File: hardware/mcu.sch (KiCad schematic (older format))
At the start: 4 parts

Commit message: HW: change tm4c1294ncpdt to kcpdt; change LT3487 to 3471
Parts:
- removed U? (x4): TM4C1294NCPDT, symbol TM4C1294NCPDT
- added U? (x4): TM4C1294KCPDT, symbol TM4C1294KCPDT
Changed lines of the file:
@@
 Text HLabel 10400 2950 0    60   Output ~ 0
 PWM2
-$Comp
-L TM4C1294NCPDT U?
-U 1 1 597FCC05
-P 1450 2650
-F 0 "U?" H 1400 1000 59  0000 C CNN
-F 1 "TM4C1294NCPDT" H 1450 4400 59  0000 C CNN
-F 2 "" H 1400 1400 59  0000 C CNN
-F 3 "" H 1400 1400 59  0000 C CNN
-	1    1450 2650
-	1    0    0    -1
-$EndComp
-$Comp
-L TM4C1294NCPDT U?
-U 2 1 597FCCB0
-P 4400 2350
-F 0 "U?" H 4400 1050 59  0000 C CNN
-F 1 "TM4C1294NCPDT" H 4400 3500 59  0000 C CNN
-F 2 "" H 4350 1100 59  0000 C CNN
-F 3 "" H 4350 1100 59  0000 C CNN
-	2    4400 2350
-	1    0    0    -1
-$EndComp
-$Comp
-L TM4C1294NCPDT U?
-U 3 1 597FCD49
-P 6750 1700
-F 0 "U?" H 6800 1250 59  0000 C CNN
-F 1 "TM4C1294NCPDT" H 6800 2100 59  0000 C CNN
-F 2 "" H 6700 450 59  0000 C CNN
-F 3 "" H 6700 450 59  0000 C CNN
-	3    6750 1700
-	1    0    0    -1
-$EndComp
-$Comp
-L TM4C1294NCPDT U?
-U 4 1 597FCDA0
-P 9100 2300
-F 0 "U?" H 9100 1100 59  0000 C CNN
-F 1 "TM4C1294NCPDT" H 9100 3350 59  0000 C CNN
-F 2 "" H 9050 1050 59  0000 C CNN
-F 3 "" H 9050 1050 59  0000 C CNN
-	4    9100 2300
-	1    0    0    -1
-$EndComp
 Wire Wire Line
 	9700 1350 9800 1350
@@
 Text Notes 6000 6350 2    197  ~ 0
 STATUS LEDs
+$Comp
+L TM4C1294KCPDT U?
+U 1 1 59940BF1
+P 1800 2600
+F 0 "U?" H 1750 950 59  0000 C CNN
+F 1 "TM4C1294KCPDT" H 1800 4350 59  0000 C CNN
+F 2 "" H 1750 1350 59  0000 C CNN
+F 3 "" H 1750 1350 59  0000 C CNN
+	1    1800 2600
+	1    0    0    -1
+$EndComp
+$Comp
+L TM4C1294KCPDT U?
+U 2 1 59940C7A
+P 3800 2200
+F 0 "U?" H 3800 850 59  0000 C CNN
+F 1 "TM4C1294KCPDT" H 3800 3400 59  0000 C CNN
+F 2 "" H 3750 950 59  0000 C CNN
+F 3 "" H 3750 950 59  0000 C CNN
+	2    3800 2200
+	1    0    0    -1
+$EndComp
+$Comp
+L TM4C1294KCPDT U?
+U 3 1 59940CC3
+P 6100 2250
+F 0 "U?" H 6150 1750 59  0000 C CNN
+F 1 "TM4C1294KCPDT" H 6150 2700 59  0000 C CNN
+F 2 "" H 6050 1000 59  0000 C CNN
+F 3 "" H 6050 1000 59  0000 C CNN
+	3    6100 2250
+	1    0    0    -1
+$EndComp
+$Comp
+L TM4C1294KCPDT U?
+U 4 1 59940D20
+P 9100 2300
+F 0 "U?" H 9100 1100 59  0000 C CNN
+F 1 "TM4C1294KCPDT" H 9100 3400 59  0000 C CNN
+F 2 "" H 9050 1050 59  0000 C CNN
+F 3 "" H 9050 1050 59  0000 C CNN
+	4    9100 2300
+	1    0    0    -1
+$EndComp
 $EndSCHEMATC

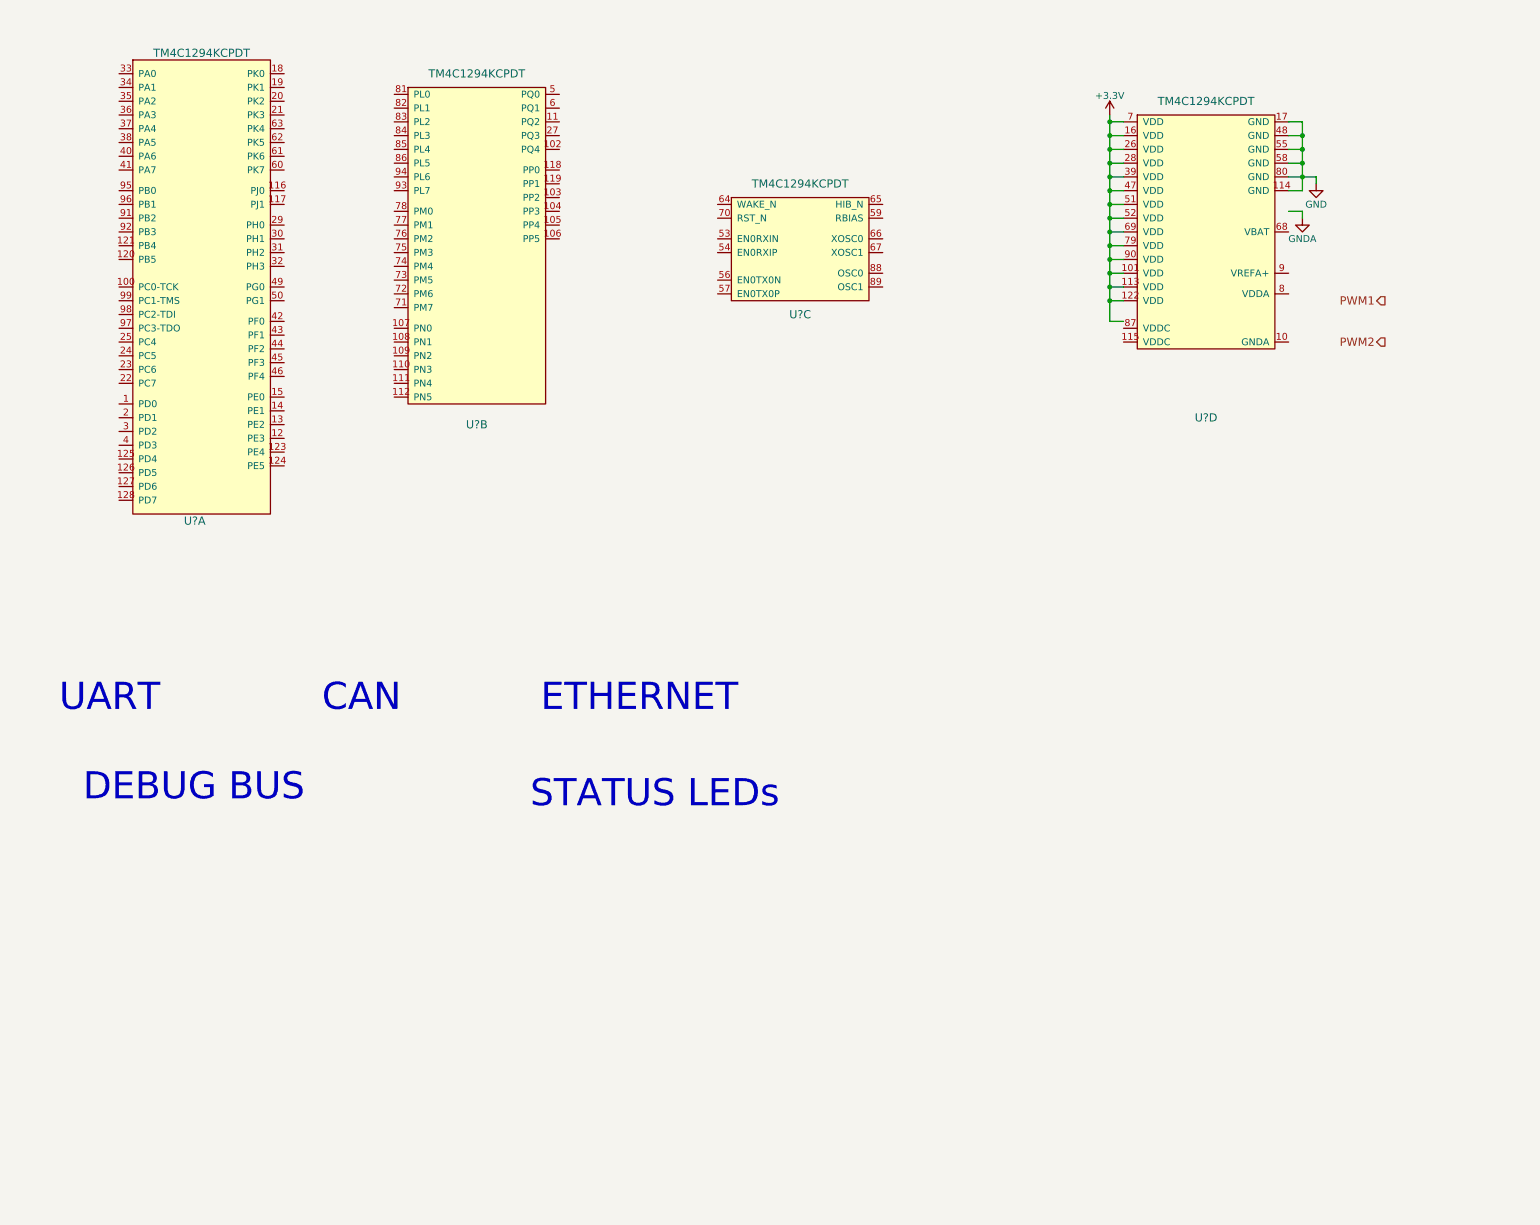
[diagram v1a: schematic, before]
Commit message: cleaned up h-bridge; added digital isolators
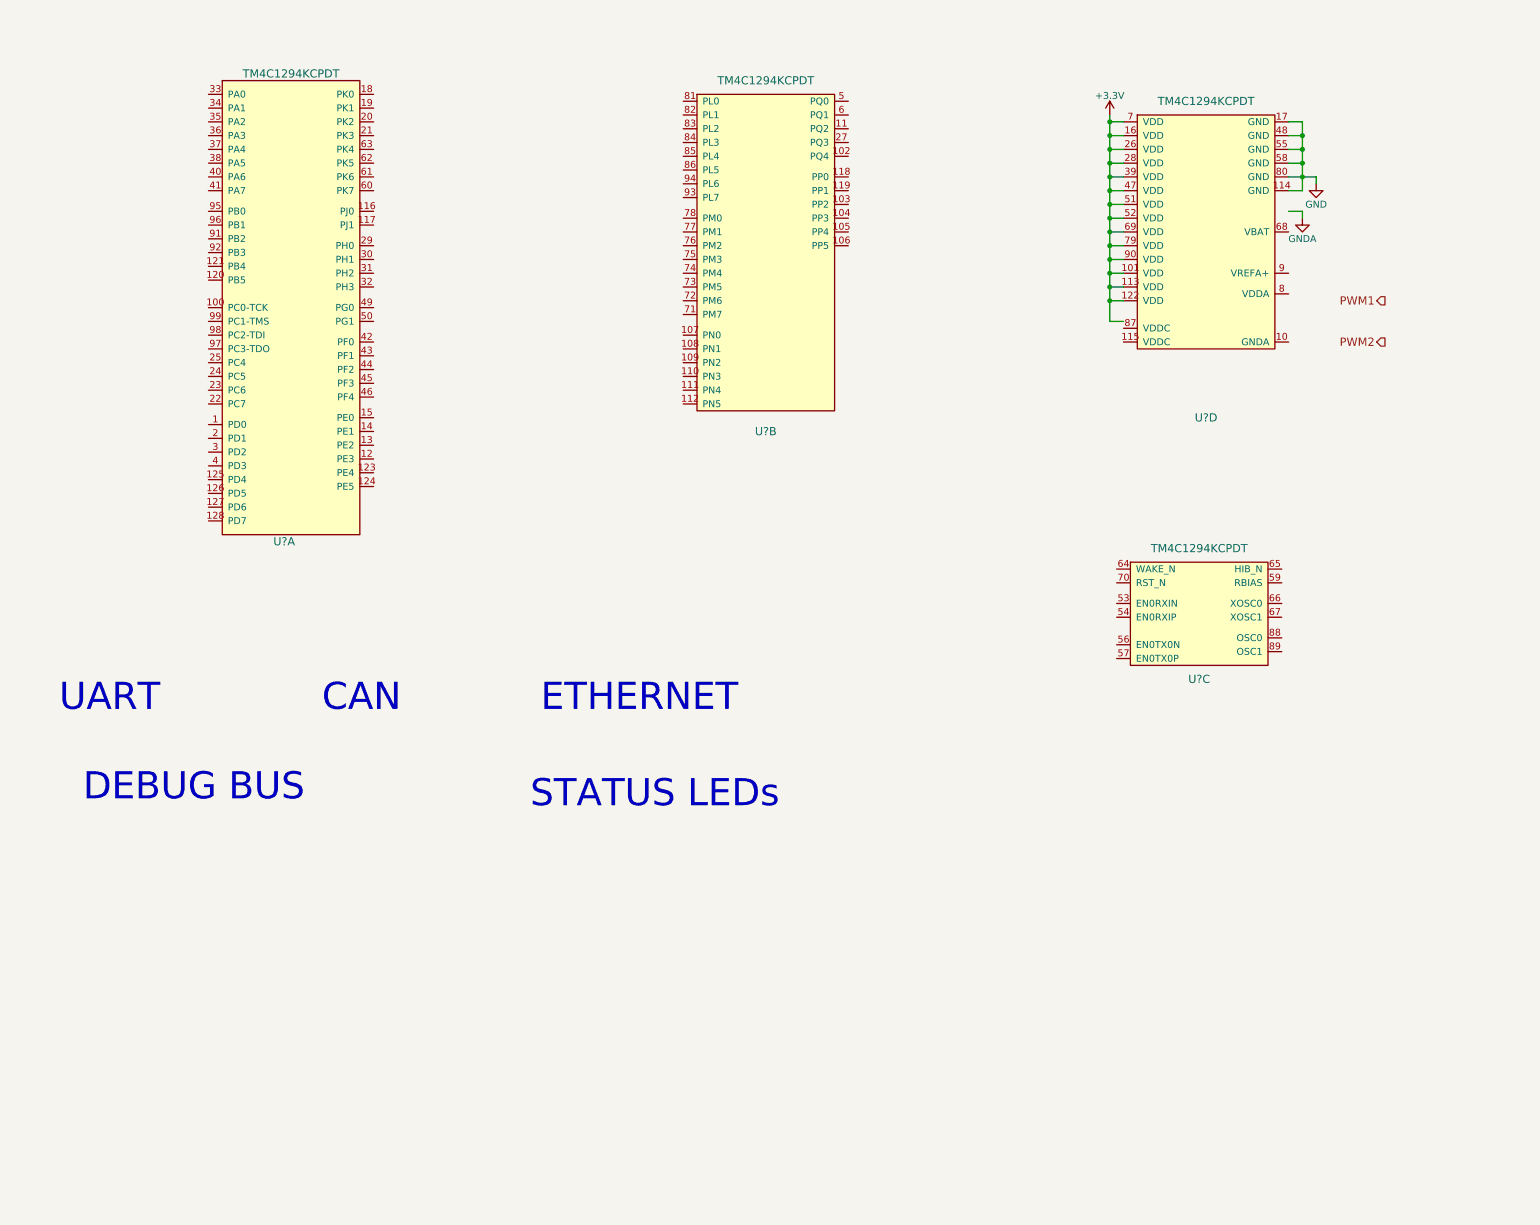
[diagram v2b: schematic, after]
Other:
- moved on the sheet: U?A, U?B, U?C
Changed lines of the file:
@@
 Connection ~ 9800 1450
 $Comp
-L GND #PWR?
+L GND #PWR07
 U 1 1 5983EA5A
 P 9900 1800
-F 0 "#PWR?" H 9900 1550 50  0001 C CNN
+F 0 "#PWR07" H 9900 1550 50  0001 C CNN
 F 1 "GND" H 9900 1650 50  0000 C CNN
 F 2 "" H 9900 1800 50  0000 C CNN
@@
 	9800 2000 9800 2050
 $Comp
-L GNDA #PWR?
+L GNDA #PWR08
 U 1 1 5983EB4E
 P 9800 2050
-F 0 "#PWR?" H 9800 1800 50  0001 C CNN
+F 0 "#PWR08" H 9800 1800 50  0001 C CNN
 F 1 "GNDA" H 9800 1900 50  0000 C CNN
 F 2 "" H 9800 2050 50  0000 C CNN
@@
 $EndComp
 $Comp
-L +3.3V #PWR?
+L +3.3V #PWR09
 U 1 1 5983EC7E
 P 8400 1300
-F 0 "#PWR?" H 8400 1150 50  0001 C CNN
+F 0 "#PWR09" H 8400 1150 50  0001 C CNN
 F 1 "+3.3V" H 8400 1440 50  0000 C CNN
 F 2 "" H 8400 1300 50  0000 C CNN
@@
 L TM4C1294KCPDT U?
 U 1 1 59940BF1
-P 1800 2600
-F 0 "U?" H 1750 950 59  0000 C CNN
-F 1 "TM4C1294KCPDT" H 1800 4350 59  0000 C CNN
-F 2 "" H 1750 1350 59  0000 C CNN
-F 3 "" H 1750 1350 59  0000 C CNN
-	1    1800 2600
+P 2450 2750
+F 0 "U?" H 2400 1100 59  0000 C CNN
+F 1 "TM4C1294KCPDT" H 2450 4500 59  0000 C CNN
+F 2 "" H 2400 1500 59  0000 C CNN
+F 3 "" H 2400 1500 59  0000 C CNN
+	1    2450 2750
 	1    0    0    -1
 $EndComp
@@
 L TM4C1294KCPDT U?
 U 2 1 59940C7A
-P 3800 2200
-F 0 "U?" H 3800 850 59  0000 C CNN
-F 1 "TM4C1294KCPDT" H 3800 3400 59  0000 C CNN
-F 2 "" H 3750 950 59  0000 C CNN
-F 3 "" H 3750 950 59  0000 C CNN
-	2    3800 2200
+P 5900 2250
+F 0 "U?" H 5900 900 59  0000 C CNN
+F 1 "TM4C1294KCPDT" H 5900 3450 59  0000 C CNN
+F 2 "" H 5850 1000 59  0000 C CNN
+F 3 "" H 5850 1000 59  0000 C CNN
+	2    5900 2250
 	1    0    0    -1
 $EndComp
@@
 L TM4C1294KCPDT U?
 U 3 1 59940CC3
-P 6100 2250
-F 0 "U?" H 6150 1750 59  0000 C CNN
-F 1 "TM4C1294KCPDT" H 6150 2700 59  0000 C CNN
-F 2 "" H 6050 1000 59  0000 C CNN
-F 3 "" H 6050 1000 59  0000 C CNN
-	3    6100 2250
+P 9000 4900
+F 0 "U?" H 9050 4400 59  0000 C CNN
+F 1 "TM4C1294KCPDT" H 9050 5350 59  0000 C CNN
+F 2 "" H 8950 3650 59  0000 C CNN
+F 3 "" H 8950 3650 59  0000 C CNN
+	3    9000 4900
 	1    0    0    -1
 $EndComp

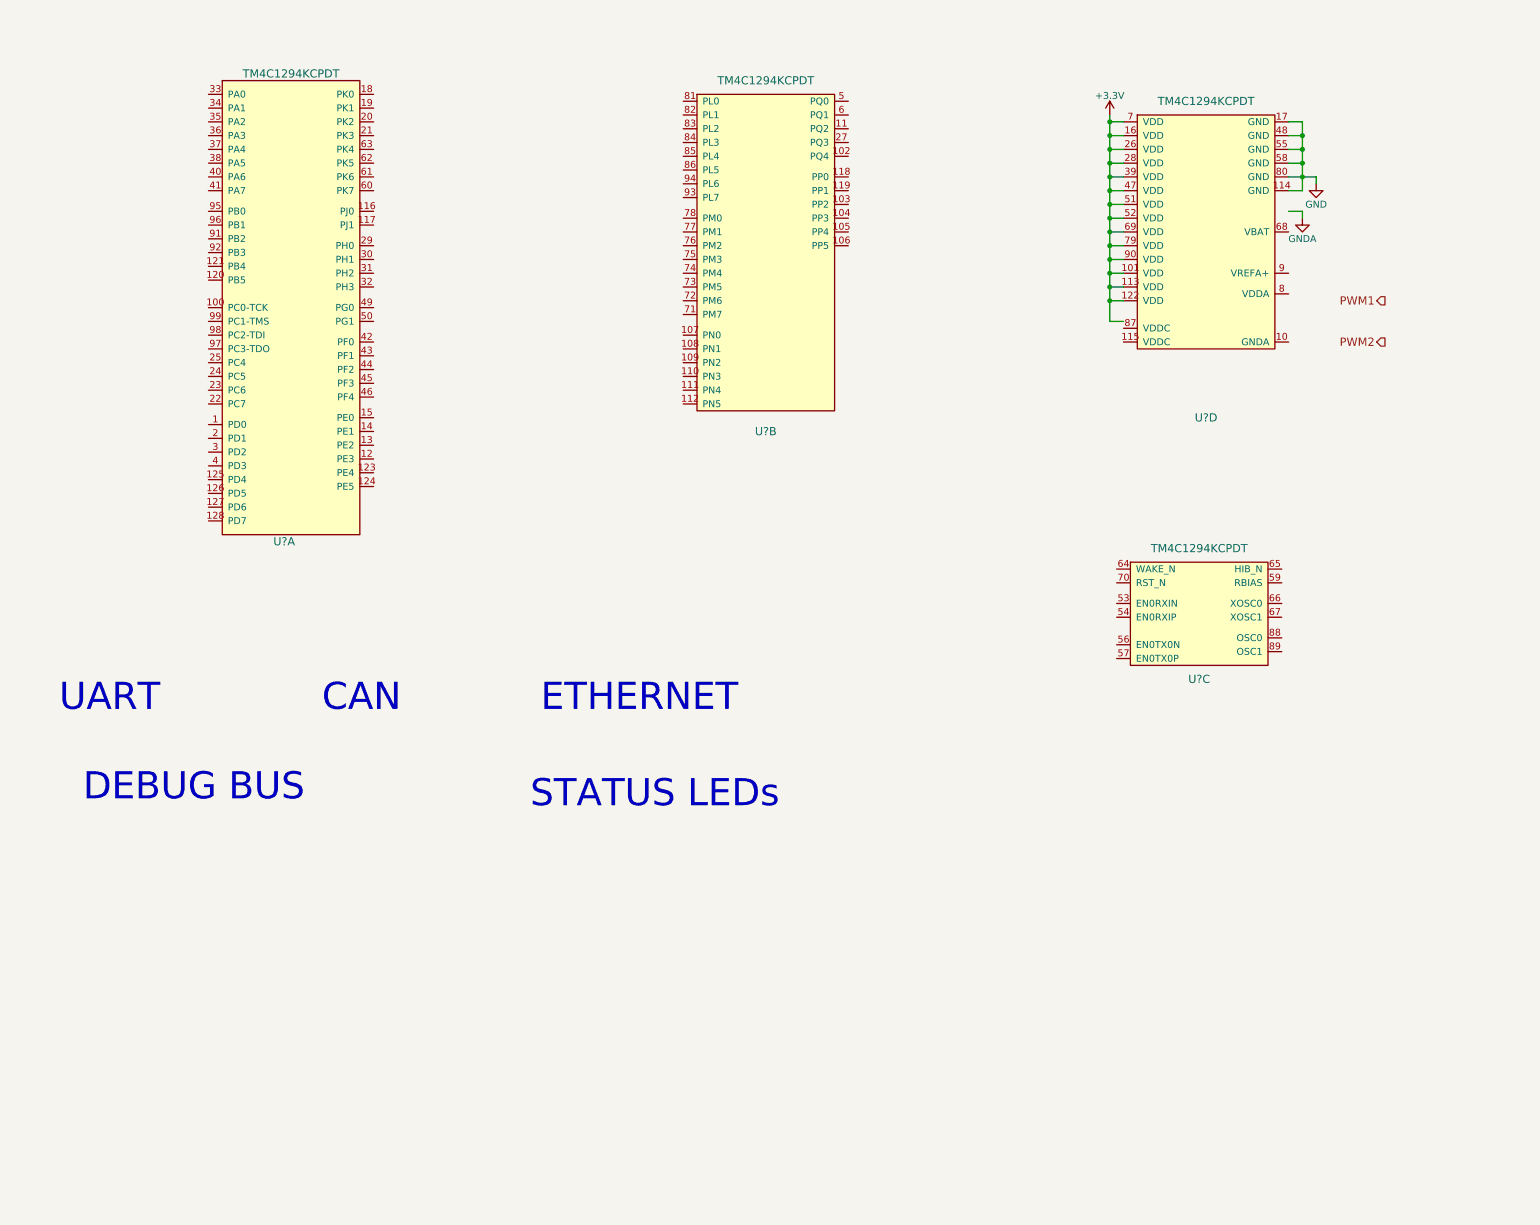
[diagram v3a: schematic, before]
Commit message: added MCU caps, reset, jtag, crystal
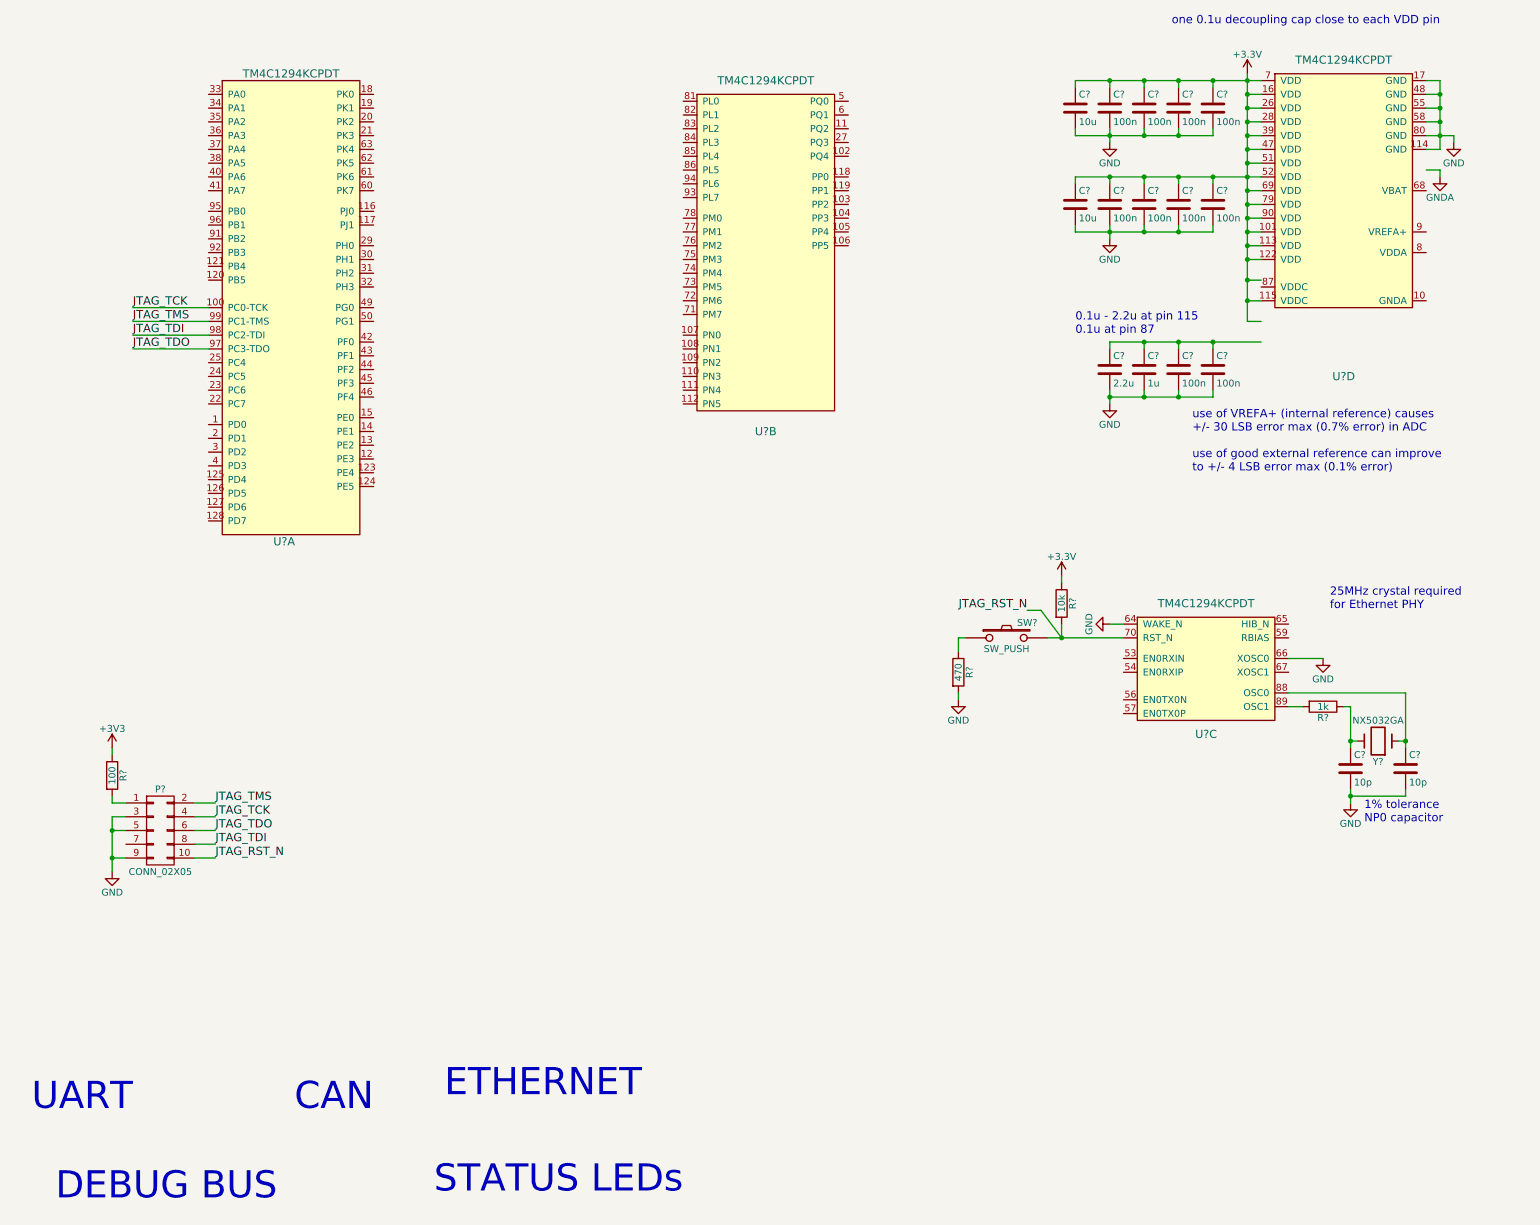
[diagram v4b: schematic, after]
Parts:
- added C? (x10): 100n, symbol C
- added C?: 1u, symbol C
- added C?: 2.2u, symbol C
- added C? (x2): 10u, symbol C
- added C? (x2): 10p, symbol C
- added P?: CONN_02X05, symbol CONN_02X05
- added R?: 470, symbol R
- added R?: 10k, symbol R
- added R?: 1k, symbol R
- added R?: 100, symbol R
- added SW?: SW_PUSH, symbol SW_PUSH
- added Y?: NX5032GA, symbol Crystal
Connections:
- net labels added: +3V3, JTAG_RST_N, JTAG_TCK, JTAG_TDI, JTAG_TDO, JTAG_TMS
- net labels removed: PWM1, PWM2
- wire segments 26 -> 147
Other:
- note added: "0.1u - 2.2u at pin 115\n0.1u at pin 87"
- note added: "1% tolerance\nNP0 capacitor"
- note added: "25MHz crystal required\nfor Ethernet PHY"
- note added: "one 0.1u decoupling cap close to each VDD pin"
- note added: "use of VREFA+ (internal reference) causes\n+/- 30 LSB error max (0.7% error) in ADC\n\nuse of good external reference can improve\nto +/- 4 LSB error max (0.1% error)"
- moved on the sheet: U?C, U?D
